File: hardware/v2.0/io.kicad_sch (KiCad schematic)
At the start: 1 part, among them U1 ECP5U-25F-CABGA256

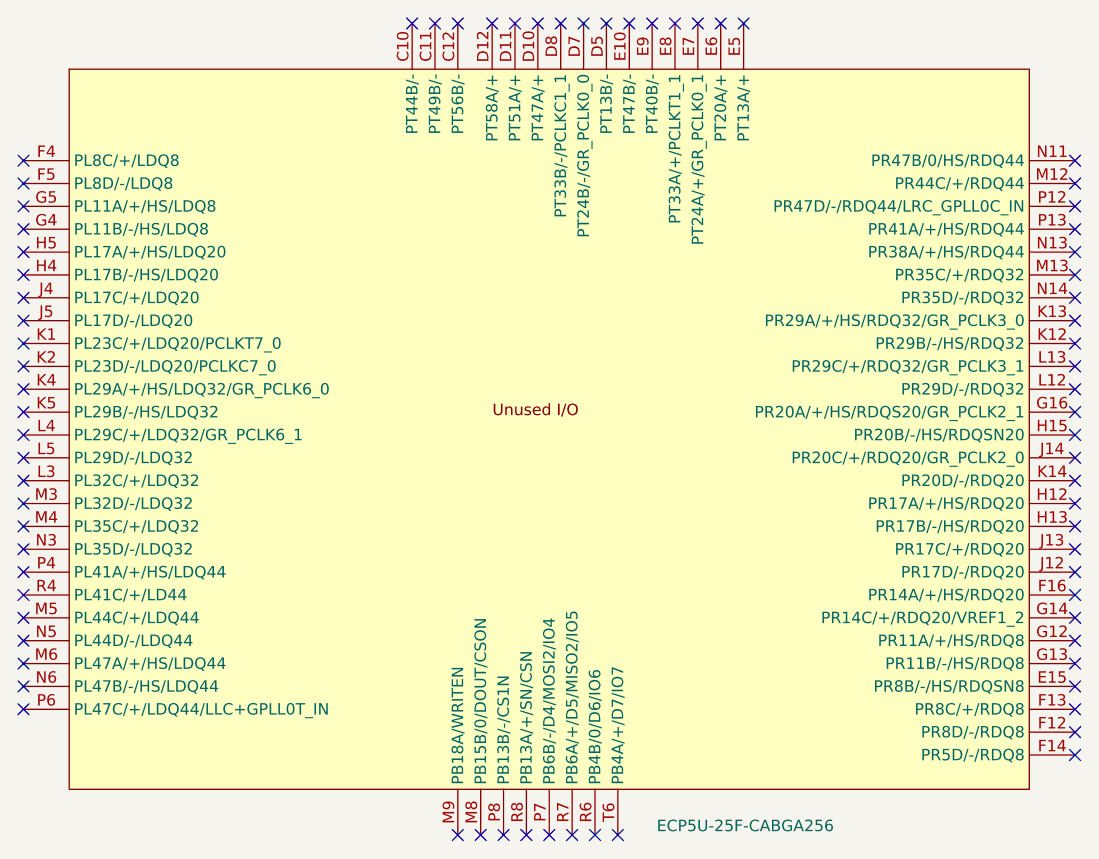
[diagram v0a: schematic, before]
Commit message: ADC 6 diff lines
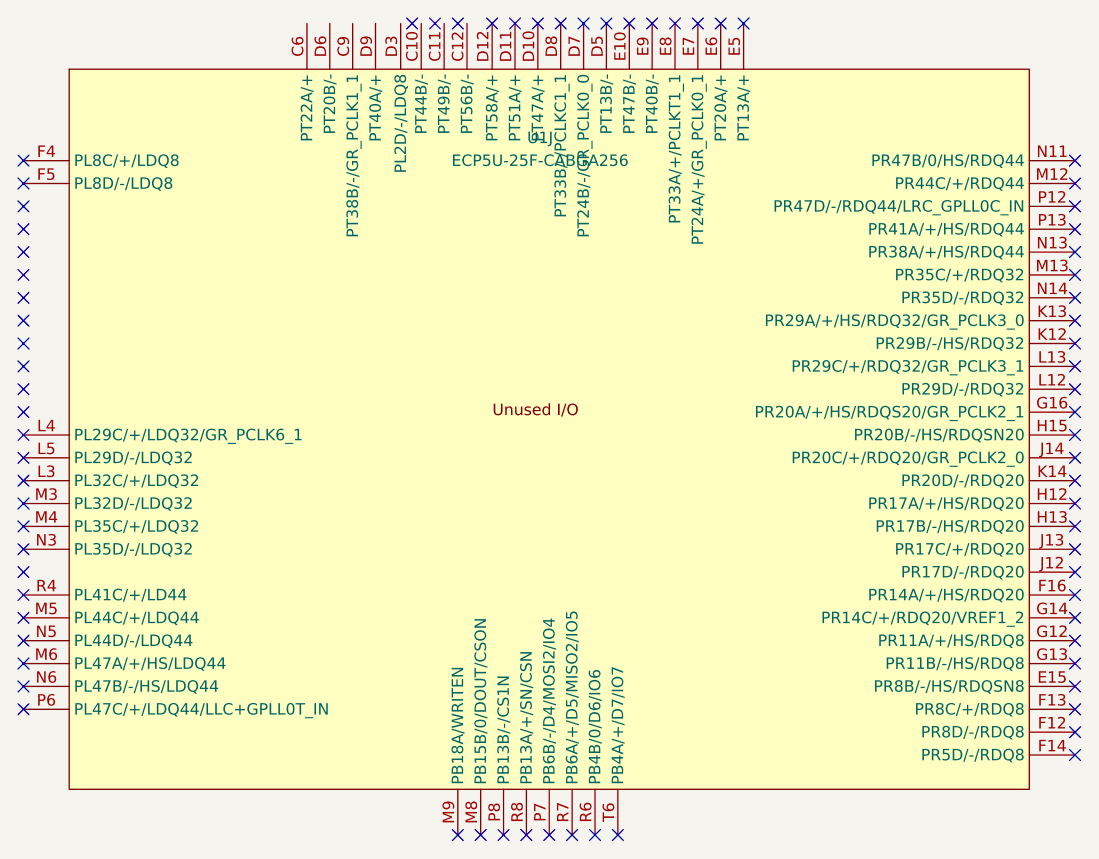
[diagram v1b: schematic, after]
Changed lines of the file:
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@@
 		(dnp no)
 		(property "Reference" "U1"
-			(at 154.432 26.162 0)
+			(at 155.194 63.5 0)
 			(effects
 				(font
 					(size 1.27 1.27)
 				)
-				(hide yes)
 			)
 		)
 		(property "Value" "ECP5U-25F-CABGA256"
-			(at 168.148 139.954 0)
+			(at 155.194 66.04 0)
 			(effects
 				(font
 					(size 1.27 1.27)
 				)
-				(justify left)
 			)
 		)
@@
 					(reference "U1")
 					(unit 10)
+				)
+				(path "/f88da08e-cf42-4d03-a08f-3f602fe6658d/b5a9aa02-311b-4a9a-a7d4-646f15cdd9c2"
+					(reference "U1")
+					(unit 10)

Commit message: ADC lines
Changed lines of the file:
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@@
-					(unit 10)
-				)
-				(path "/f88da08e-cf42-4d03-a08f-3f602fe6658d/b5a9aa02-311b-4a9a-a7d4-646f15cdd9c2"
-					(reference "U1")
 					(unit 10)
 				)

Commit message: ADC CLKOUT±
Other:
- company: Chengyin Yao (cheyao), Vadym Vikulin -> Vadym Vikulin, Chengyin Yao (cheyao)
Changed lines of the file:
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@@
 	(title_block
 		(title "Icepi Zero")
-		(date "2026-01-05")
-		(rev "v2.0")
-		(company "Chengyin Yao (cheyao), Vadym Vikulin")
-		(comment 1 "https://github.com/cheyao/icepi-zero")
+		(date "2026-01-17")
+		(rev "v2.1")
+		(company "Vadym Vikulin, Chengyin Yao (cheyao)")
+		(comment 1 "https://github.com/vikulin/icepi-zero")
 		(comment 2 "License: Solderpad")
 		(comment 9 "OSHWA FR000026")
@@
 		(pin "P11"
 		)
+		(pin "N6"
+		)
 		(instances

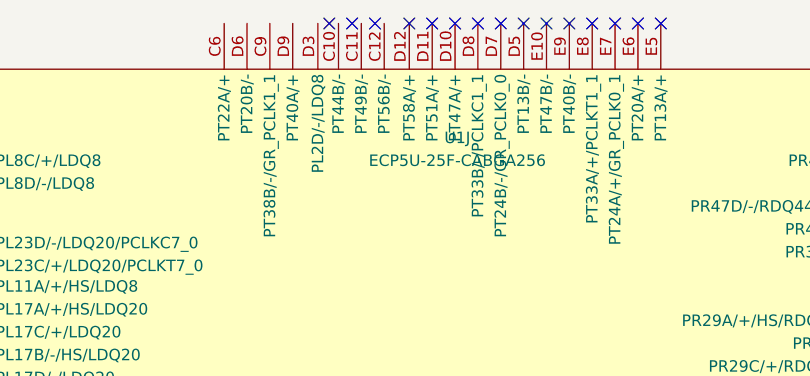
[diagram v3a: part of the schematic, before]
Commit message: ADC driver enable pin
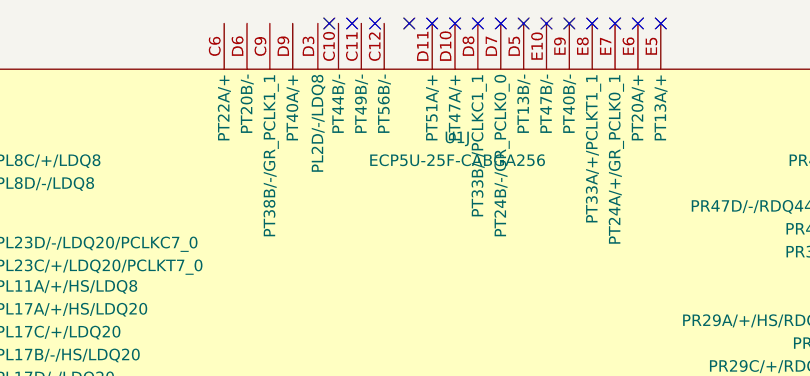
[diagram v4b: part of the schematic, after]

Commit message: ADC SPI SDO
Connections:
- no-connect marks 75 -> 70
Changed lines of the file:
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@@
-	)
-	(no_connect
-		(at 140.97 50.8)
 	)
 	(no_connect
@@
 	)
 	(no_connect
-		(at 97.79 68.58)
-	)
-	(no_connect
 		(at 154.94 50.8)
 	)
@@
 	)
 	(no_connect
-		(at 97.79 71.12)
-	)
-	(no_connect
 		(at 156.21 140.97)
 	)
@@
 	)
 	(no_connect
-		(at 97.79 111.76)
-	)
-	(no_connect
 		(at 214.63 68.58)
 	)
@@
 	)
 	(no_connect
+		(at 136.906 50.8)
+	)
+	(no_connect
+		(at 98.298 75.184)
+	)
+	(no_connect
 		(at 214.63 83.82)
 	)
@@
 	)
 	(no_connect
-		(at 97.79 93.98)
-	)
-	(no_connect
-		(at 97.79 109.22)
+		(at 134.366 50.8)
+	)
+	(no_connect
+		(at 98.298 85.09)
 	)
 	(no_connect
@@
 	)
 	(no_connect
-		(at 97.79 124.46)
-	)
-	(no_connect
-		(at 97.79 99.06)
-	)
-	(no_connect
-		(at 97.79 78.74)
-	)
-	(no_connect
 		(at 214.63 129.54)
 	)
 	(no_connect
-		(at 146.05 50.8)
-	)
-	(no_connect
 		(at 148.59 140.97)
 	)
 	(no_connect
+		(at 98.298 96.52)
+	)
+	(no_connect
 		(at 214.63 101.6)
 	)
@@
 	)
 	(no_connect
+		(at 139.7 50.8)
+	)
+	(no_connect
 		(at 214.63 111.76)
 	)
 	(no_connect
-		(at 149.86 50.8)
-	)
-	(no_connect
-		(at 97.79 116.84)
-	)
-	(no_connect
 		(at 214.63 124.46)
 	)
@@
 	)
 	(no_connect
-		(at 97.79 76.2)
-	)
-	(no_connect
-		(at 97.79 91.44)
-	)
-	(no_connect
-		(at 97.79 83.82)
+		(at 98.298 99.06)
+	)
+	(no_connect
+		(at 98.298 106.68)
 	)
 	(no_connect
@@
 	)
 	(no_connect
-		(at 97.79 88.9)
-	)
-	(no_connect
-		(at 97.79 121.92)
-	)
-	(no_connect
-		(at 97.79 86.36)
-	)
-	(no_connect
-		(at 143.51 50.8)
-	)
-	(no_connect
 		(at 214.63 99.06)
 	)
 	(no_connect
-		(at 97.79 66.04)
+		(at 98.298 119.38)
+	)
+	(no_connect
+		(at 98.298 127)
+	)
+	(no_connect
+		(at 129.286 50.8)
 	)
 	(no_connect
@@
 	)
 	(no_connect
-		(at 97.79 73.66)
-	)
-	(no_connect
 		(at 158.75 140.97)
 	)
 	(no_connect
-		(at 97.79 81.28)
-	)
-	(no_connect
 		(at 151.13 140.97)
 	)
@@
 	)
 	(no_connect
-		(at 97.79 127)
-	)
-	(no_connect
 		(at 214.63 71.12)
 	)
 	(no_connect
-		(at 97.79 114.3)
-	)
-	(no_connect
 		(at 214.63 132.08)
 	)
@@
 	)
 	(no_connect
+		(at 144.526 50.8)
+	)
+	(no_connect
+		(at 98.298 82.55)
+	)
+	(no_connect
 		(at 161.29 140.97)
 	)
@@
 	)
 	(no_connect
-		(at 97.79 106.68)
+		(at 98.298 124.46)
+	)
+	(no_connect
+		(at 98.298 109.22)
+	)
+	(no_connect
+		(at 98.298 90.17)
+	)
+	(no_connect
+		(at 98.298 116.84)
+	)
+	(no_connect
+		(at 98.298 68.58)
 	)
 	(no_connect
@@
 	)
 	(no_connect
+		(at 98.298 77.724)
+	)
+	(no_connect
+		(at 98.298 87.63)
+	)
+	(no_connect
 		(at 214.63 109.22)
 	)
 	(no_connect
+		(at 131.826 50.8)
+	)
+	(no_connect
 		(at 214.63 119.38)
 	)
 	(no_connect
+		(at 141.986 50.8)
+	)
+	(no_connect
 		(at 214.63 73.66)
 	)
 	(no_connect
-		(at 97.79 101.6)
-	)
-	(no_connect
-		(at 97.79 119.38)
+		(at 98.298 66.04)
 	)
 	(no_connect
@@
 	)
 	(no_connect
-		(at 97.79 104.14)
+		(at 98.298 80.01)
 	)
 	(no_connect
@@
 	)
 	(no_connect
-		(at 97.79 96.52)
-	)
-	(no_connect

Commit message: BOM fields unification for PCBWay requirements
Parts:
- U1: MANUFACTURER (none) -> Lattice; MANUFACTURER_PART_NUMBER (none) -> LFE5U-25F-6BG256C
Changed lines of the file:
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@@
+			)
+		)
+		(property "Original" ""
+			(at 156.21 93.98 0)
+			(effects
+				(font
+					(size 1.27 1.27)
+				)
+				(hide yes)
+			)
+		)
+		(property "Instructions/Notes" ""
+			(at 156.21 93.98 0)
+			(effects
+				(font
+					(size 1.27 1.27)
+				)
+				(hide yes)
+			)
+		)
+		(property "MANUFACTURER" "Lattice"
+			(at 156.21 93.98 0)
+			(effects
+				(font
+					(size 1.27 1.27)
+				)
+				(hide yes)
+			)
+		)
+		(property "MANUFACTURER_PART_NUMBER" "LFE5U-25F-6BG256C"
+			(at 156.21 93.98 0)
+			(effects
+				(font
+					(size 1.27 1.27)
+				)
+				(hide yes)
 			)
 		)
